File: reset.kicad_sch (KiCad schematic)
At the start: 45 parts, among them J7 JST_SH_1x8_BM08B-SRSS-TB-LF-SN, Q8 DTC014T_SOT-416, Q9 DTC014T_SOT-416, U31 TPS3840PH30DBVR, U32 TPS3840PH30DBVR, U33 74AVC4T245_UQFN, U34 SN74AVC2T245_UQFN, U35 SN74LVC1G125_SOT, U36 74LCX07_QFN

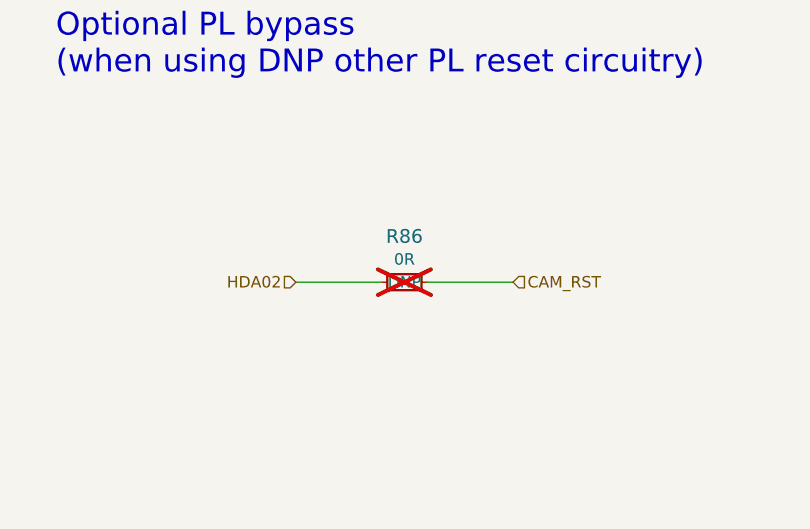
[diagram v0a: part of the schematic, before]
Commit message: Replaced LVDS connector with correct one and started pinning it out
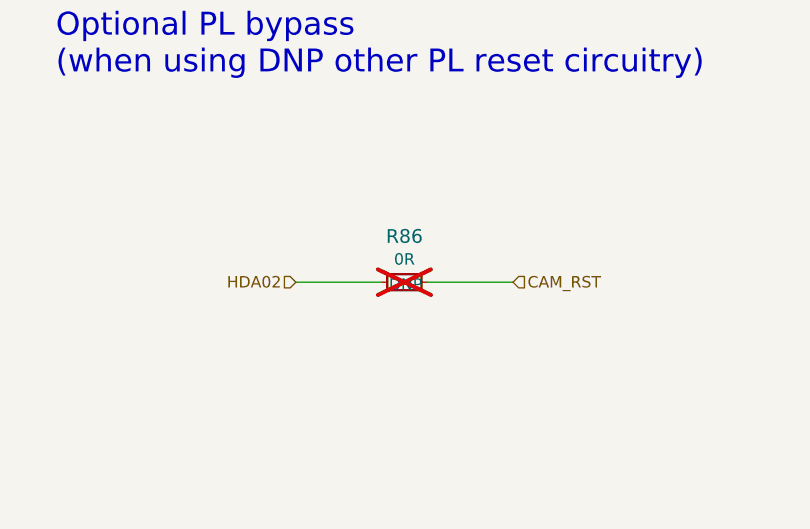
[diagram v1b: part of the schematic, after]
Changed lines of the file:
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@@
 		)
 		(property "DNP" "DNP"
-			(at 197.485 259.08 0)
+			(at 197.612 259.334 0)
 			(effects
 				(font

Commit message: swapped footprint for level shifter IC, modified ethernet footprint hole diameter
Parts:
- U36: footprint kria-k26-devboard-footprints:QFN-14-1EP_2.5x3mm_EP1.15x1.65mm_ONSemi_MLP14A -> kria-k26-devboard-footprints:74LVC07ABQ_115
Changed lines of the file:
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@@
 			)
 		)
-		(property "Footprint" "kria-k26-devboard-footprints:QFN-14-1EP_2.5x3mm_EP1.15x1.65mm_ONSemi_MLP14A"
+		(property "Footprint" "kria-k26-devboard-footprints:74LVC07ABQ_115"
 			(at 295.91 119.38 0)
 			(effects
@@
 			)
 		)
-		(property "Footprint" "kria-k26-devboard-footprints:QFN-14-1EP_2.5x3mm_EP1.15x1.65mm_ONSemi_MLP14A"
+		(property "Footprint" "kria-k26-devboard-footprints:74LVC07ABQ_115"
 			(at 295.91 100.33 0)
 			(effects
@@
 			)
 		)
-		(property "Footprint" "kria-k26-devboard-footprints:QFN-14-1EP_2.5x3mm_EP1.15x1.65mm_ONSemi_MLP14A"
+		(property "Footprint" "kria-k26-devboard-footprints:74LVC07ABQ_115"
 			(at 295.91 87.63 0)
 			(effects
@@
 			)
 		)
-		(property "Footprint" "kria-k26-devboard-footprints:QFN-14-1EP_2.5x3mm_EP1.15x1.65mm_ONSemi_MLP14A"
+		(property "Footprint" "kria-k26-devboard-footprints:74LVC07ABQ_115"
 			(at 295.91 74.93 0)
 			(effects
@@
 			)
 		)
-		(property "Footprint" "kria-k26-devboard-footprints:QFN-14-1EP_2.5x3mm_EP1.15x1.65mm_ONSemi_MLP14A"
+		(property "Footprint" "kria-k26-devboard-footprints:74LVC07ABQ_115"
 			(at 295.91 62.23 0)
 			(effects
@@
 			)
 		)
-		(property "Footprint" "kria-k26-devboard-footprints:QFN-14-1EP_2.5x3mm_EP1.15x1.65mm_ONSemi_MLP14A"
+		(property "Footprint" "kria-k26-devboard-footprints:74LVC07ABQ_115"
 			(at 331.47 144.78 0)
 			(effects
@@
 			)
 		)
-		(property "Footprint" "kria-k26-devboard-footprints:QFN-14-1EP_2.5x3mm_EP1.15x1.65mm_ONSemi_MLP14A"
+		(property "Footprint" "kria-k26-devboard-footprints:74LVC07ABQ_115"
 			(at 295.91 134.62 0)
 			(effects
